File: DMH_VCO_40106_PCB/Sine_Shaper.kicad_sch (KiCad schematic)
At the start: 13 parts, among them Q5 2N3904, Q6 2N3904, U3 TL072

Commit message: Added Cermet 3296W fp to trimpots
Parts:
- RV10, RV9: footprint (none) -> Potentiometer_THT:Potentiometer_Bourns_3296W_Vertical
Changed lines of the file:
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@@
 			)
 		)
-		(property "Footprint" ""
+		(property "Footprint" "Potentiometer_THT:Potentiometer_Bourns_3296W_Vertical"
 			(at 120.65 115.57 0)
 			(effects
@@
 			)
 		)
-		(property "Footprint" ""
+		(property "Footprint" "Potentiometer_THT:Potentiometer_Bourns_3296W_Vertical"
 			(at 82.55 87.63 0)
 			(effects

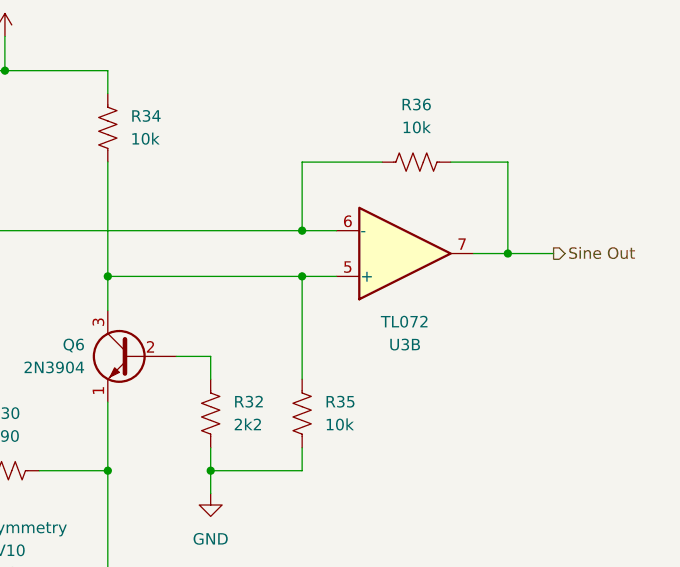
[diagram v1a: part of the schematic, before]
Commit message: Made U3 into TL074 instead of TL072
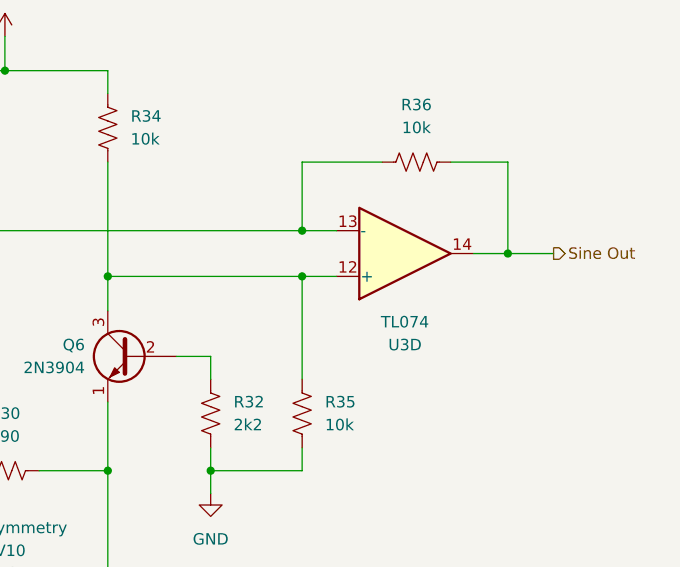
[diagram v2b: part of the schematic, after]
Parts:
- removed U3: TL072, Package_DIP:DIP-8_W7.62mm_Socket, symbol Amplifier_Operational:TL072
- added U3: TL074, symbol Amplifier_Operational:TL074
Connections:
- net Sine Out: now also U3.14
- net at Q5.3 (C), R33.2, R36.1: now also U3.13 (-)
- net at Q6.3 (C), R34.2, R35.1: now also U3.12 (+)
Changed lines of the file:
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@@
+	)
+	(symbol
+		(lib_id "Amplifier_Operational:TL074")
+		(at 165.1 76.2 0)
+		(mirror x)
+		(unit 4)
+		(exclude_from_sim no)
+		(in_bom yes)
+		(on_board yes)
+		(dnp no)
+		(property "Reference" "U3"
+			(at 165.1 86.36 0)
+			(effects
+				(font
+					(size 1.27 1.27)
+				)
+			)
+		)
+		(property "Value" "TL074"
+			(at 165.1 83.82 0)
+			(effects
+				(font
+					(size 1.27 1.27)
+				)
+			)
+		)
+		(property "Footprint" ""
+			(at 163.83 78.74 0)
+			(effects
+				(font
+					(size 1.27 1.27)
+				)
+				(hide yes)
+			)
+		)
+		(property "Datasheet" "http://www.ti.com/lit/ds/symlink/tl071.pdf"
+			(at 166.37 81.28 0)
+			(effects
+				(font
+					(size 1.27 1.27)
+				)
+				(hide yes)
+			)
+		)
+		(property "Description" "Quad Low-Noise JFET-Input Operational Amplifiers, DIP-14/SOIC-14"
+			(at 165.1 76.2 0)
+			(effects
+				(font
+					(size 1.27 1.27)
+				)
+				(hide yes)
+			)
+		)
+		(pin "9"
+		)
+		(pin "5"
+		)
+		(pin "8"
+		)
+		(pin "11"
+		)
+		(pin "10"
+		)
+		(pin "3"
+		)
+		(pin "4"
+		)
+		(pin "1"
+		)
+		(pin "12"
+		)
+		(pin "14"
+		)
+		(pin "13"
+		)
+		(pin "6"
+		)
+		(pin "2"
+		)
+		(pin "7"
+		)
+		(instances
+			(project ""
+				(path "/fefed352-c100-4617-bbfb-c55e7427b122/5d4fa276-24f5-484f-b50d-2ebe5f0666ef"
+					(reference "U3")
+					(unit 4)
+				)
+			)
+		)
 	)
 	(symbol
@@
 				)
 			)
-		)
-	)
-	(symbol
-		(lib_id "Amplifier_Operational:TL072")
-		(at 165.1 76.2 0)
-		(mirror x)
-		(unit 2)
-		(exclude_from_sim no)
-		(in_bom yes)
-		(on_board yes)
-		(dnp no)
-		(property "Reference" "U3"
-			(at 165.1 86.36 0)
-			(effects
-				(font
-					(size 1.27 1.27)
-				)
-			)
-		)
-		(property "Value" "TL072"
-			(at 165.1 83.82 0)
-			(effects
-				(font
-					(size 1.27 1.27)
-				)
-			)
-		)
-		(property "Footprint" "Package_DIP:DIP-8_W7.62mm_Socket"
-			(at 165.1 76.2 0)
-			(effects
-				(font
-					(size 1.27 1.27)
-				)
-				(hide yes)
-			)
-		)
-		(property "Datasheet" "http://www.ti.com/lit/ds/symlink/tl071.pdf"
-			(at 165.1 76.2 0)
-			(effects
-				(font
-					(size 1.27 1.27)
-				)
-				(hide yes)
-			)
-		)
-		(property "Description" "Dual Low-Noise JFET-Input Operational Amplifiers, DIP-8/SOIC-8"
-			(at 165.1 76.2 0)
-			(effects
-				(font
-					(size 1.27 1.27)
-				)
-				(hide yes)
-			)
-		)
-		(pin "2"
-		)
-		(pin "1"
-		)
-		(pin "7"
-		)
-		(pin "4"
-		)
-		(pin "6"
-		)
-		(pin "3"
-		)
-		(pin "5"
-		)
-		(pin "8"
-		)
-		(instances
-			(project "VCO mki PCB"
-				(path "/fefed352-c100-4617-bbfb-c55e7427b122/5d4fa276-24f5-484f-b50d-2ebe5f0666ef"
-					(reference "U3")
-					(unit 2)
-				)
-			)

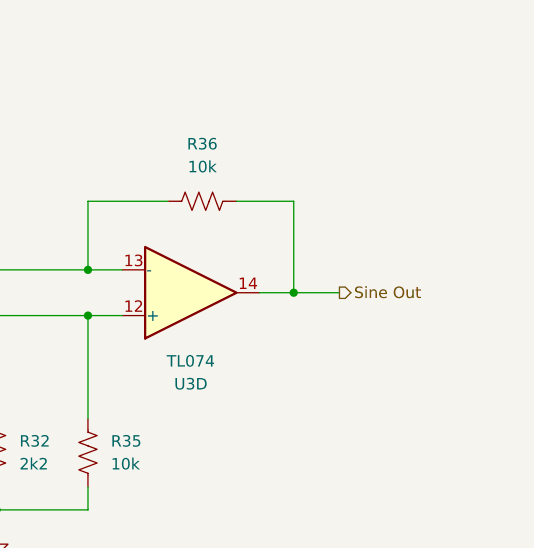
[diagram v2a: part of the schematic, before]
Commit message: Improved range of Coarse knob
... and allowed Centering knob to set C1=32,7Hz as root note with Coarse knob all the way CCW.
... and added 1kHz to Sine output.
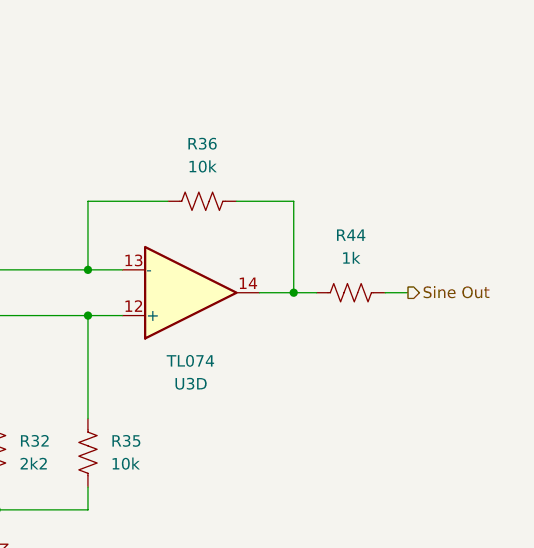
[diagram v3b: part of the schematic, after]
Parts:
- added R44: 1k, symbol Device:R_US
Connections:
- net Sine Out: now also R44.2; no longer R36.2, U3.14
- new net: R36.2, R44.1, U3.14
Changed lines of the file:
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@@
+	)
+	(junction
+		(at 132.08 100.33)
+		(diameter 0)
+		(color 0 0 0 0)
+	)
+	(junction
+		(at 143.51 100.33)
+		(diameter 0)
+		(color 0 0 0 0)
+	)
+	(junction
+		(at 76.2 87.63)
+		(diameter 0)
+		(color 0 0 0 0)
+	)
+	(junction
+		(at 109.22 100.33)
+		(diameter 0)
+		(color 0 0 0 0)
 	)
 	(junction
@@
 	)
 	(junction
-		(at 132.08 100.33)
-		(diameter 0)
-		(color 0 0 0 0)
-	)
-	(junction
-		(at 143.51 100.33)
-		(diameter 0)
-		(color 0 0 0 0)
-	)
-	(junction
-		(at 76.2 87.63)
-		(diameter 0)
-		(color 0 0 0 0)
-	)
-	(junction
-		(at 109.22 100.33)
-		(diameter 0)
-		(color 0 0 0 0)
-	)
-	(junction
 		(at 97.79 87.63)
 		(diameter 0)
@@
 	(wire
 		(pts
-			(xy 176.53 76.2) (xy 181.61 76.2)
+			(xy 186.69 76.2) (xy 189.23 76.2)
 		)
 		(stroke
@@
 		(pts
 			(xy 124.46 100.33) (xy 132.08 100.33)
+		)
+		(stroke
+			(width 0)
+			(type default)
+		)
+	)
+	(wire
+		(pts
+			(xy 176.53 76.2) (xy 179.07 76.2)
 		)
 		(stroke
@@
 	(hierarchical_label "Sine Out"
 		(shape output)
-		(at 181.61 76.2 0)
+		(at 189.23 76.2 0)
 		(fields_autoplaced yes)
 		(effects
@@
 					(unit 1)
 				)
+			)
+		)
+	)
+	(symbol
+		(lib_id "Device:R_US")
+		(at 182.88 76.2 90)
+		(unit 1)
+		(exclude_from_sim no)
+		(in_bom yes)
+		(on_board yes)
+		(dnp no)
+		(fields_autoplaced yes)
+		(property "Reference" "R44"
+			(at 182.88 69.85 90)
+			(effects
+				(font
+					(size 1.27 1.27)
+				)
+			)
+		)
+		(property "Value" "1k"
+			(at 182.88 72.39 90)
+			(effects
+				(font
+					(size 1.27 1.27)
+				)
+			)
+		)
+		(property "Footprint" ""
+			(at 183.134 75.184 90)
+			(effects
+				(font
+					(size 1.27 1.27)
+				)
+				(hide yes)
+			)
+		)
+		(property "Datasheet" "~"
+			(at 182.88 76.2 0)
+			(effects
+				(font
+					(size 1.27 1.27)
+				)
+				(hide yes)
+			)
+		)
+		(property "Description" "Resistor, US symbol"
+			(at 182.88 76.2 0)
+			(effects
+				(font
+					(size 1.27 1.27)
+				)
+				(hide yes)
+			)
+		)
+		(pin "2"
+		)
+		(pin "1"
+		)
+		(instances
+			(project "DMH_VCO_40106_PCB"
+				(path "/fefed352-c100-4617-bbfb-c55e7427b122/5d4fa276-24f5-484f-b50d-2ebe5f0666ef"
+					(reference "R44")
+					(unit 1)
+				)

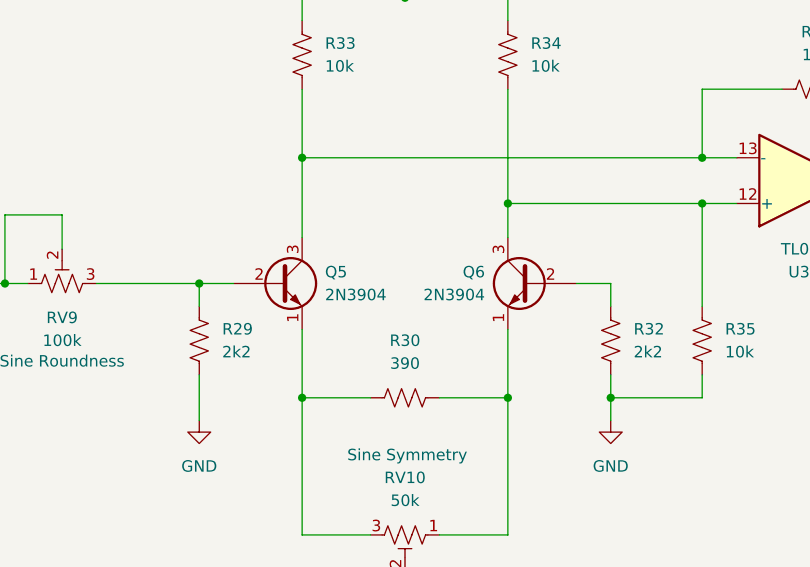
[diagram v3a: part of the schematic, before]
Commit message: Replaced 2N3904 with BC548
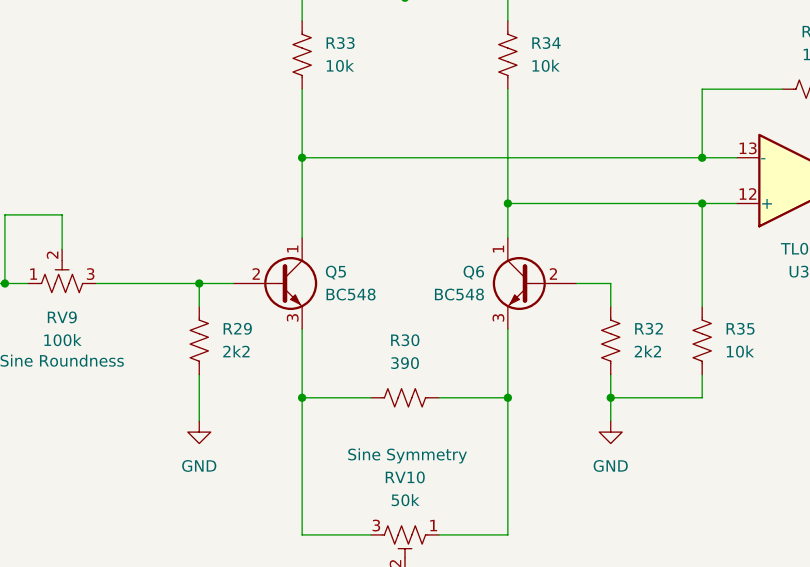
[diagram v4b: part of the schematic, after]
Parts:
- Q5, Q6: value 2N3904 -> BC548; symbol Transistor_BJT:2N3904 -> Transistor_BJT:BC548
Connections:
- net at R33.2, R36.1, U3.13 (-): now also Q5.1 (C); no longer Q5.3 (C)
- net at R30.2, RV10.1: now also Q6.3 (E); no longer Q6.1 (E)
- net at R30.1, RV10.3: now also Q5.3 (E); no longer Q5.1 (E)
- net at R34.2, R35.1, U3.12 (+): now also Q6.1 (C); no longer Q6.3 (C)
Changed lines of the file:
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@@
 	)
 	(symbol
-		(lib_id "Transistor_BJT:2N3904")
+		(lib_id "Transistor_BJT:BC548")
 		(at 106.68 87.63 0)
 		(unit 1)
@@
 			)
 		)
-		(property "Value" "2N3904"
+		(property "Value" "BC548"
 			(at 111.76 88.8999 0)
 			(effects
@@
 			)
 		)
-		(property "Datasheet" "https://www.onsemi.com/pub/Collateral/2N3903-D.PDF"
+		(property "Datasheet" "https://www.onsemi.com/pub/Collateral/BC550-D.pdf"
 			(at 106.68 87.63 0)
 			(effects
@@
 			)
 		)
-		(property "Description" "0.2A Ic, 40V Vce, Small Signal NPN Transistor, TO-92"
+		(property "Description" "0.1A Ic, 30V Vce, Small Signal NPN Transistor, TO-92"
 			(at 106.68 87.63 0)
 			(effects
@@
 	)
 	(symbol
-		(lib_id "Transistor_BJT:2N3904")
+		(lib_id "Transistor_BJT:BC548")
 		(at 134.62 87.63 0)
 		(mirror y)
@@
 			)
 		)
-		(property "Value" "2N3904"
+		(property "Value" "BC548"
 			(at 129.54 88.8999 0)
 			(effects
@@
 			)
 		)
-		(property "Datasheet" "https://www.onsemi.com/pub/Collateral/2N3903-D.PDF"
+		(property "Datasheet" "https://www.onsemi.com/pub/Collateral/BC550-D.pdf"
 			(at 134.62 87.63 0)
 			(effects
@@
 			)
 		)
-		(property "Description" "0.2A Ic, 40V Vce, Small Signal NPN Transistor, TO-92"
+		(property "Description" "0.1A Ic, 30V Vce, Small Signal NPN Transistor, TO-92"
 			(at 134.62 87.63 0)
 			(effects

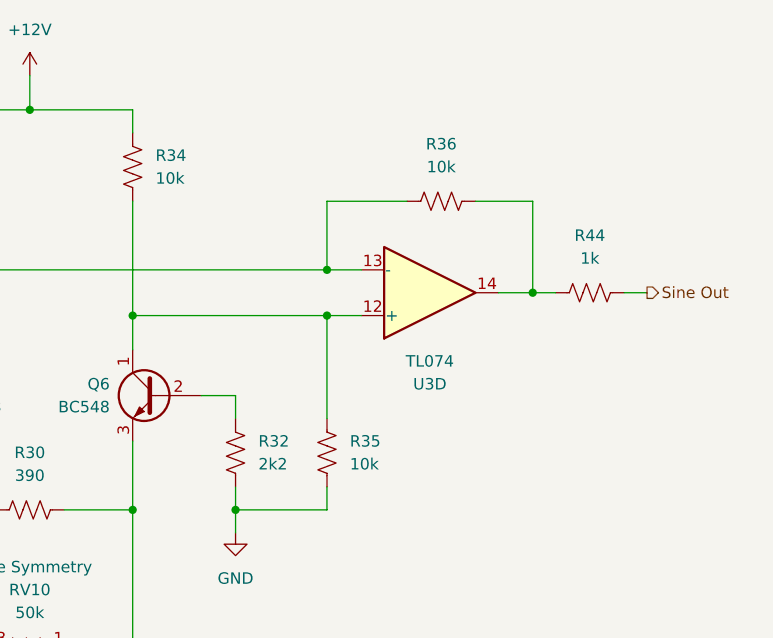
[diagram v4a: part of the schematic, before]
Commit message: Adjusted all output gains to 10Vpp
... and added buffer stages for Sawtooth Out and Triangle Out in order to avoid modifying Triangle and Sine wafeform characteristics when connecting Sawtooth Out and Triangle Out to other modules.
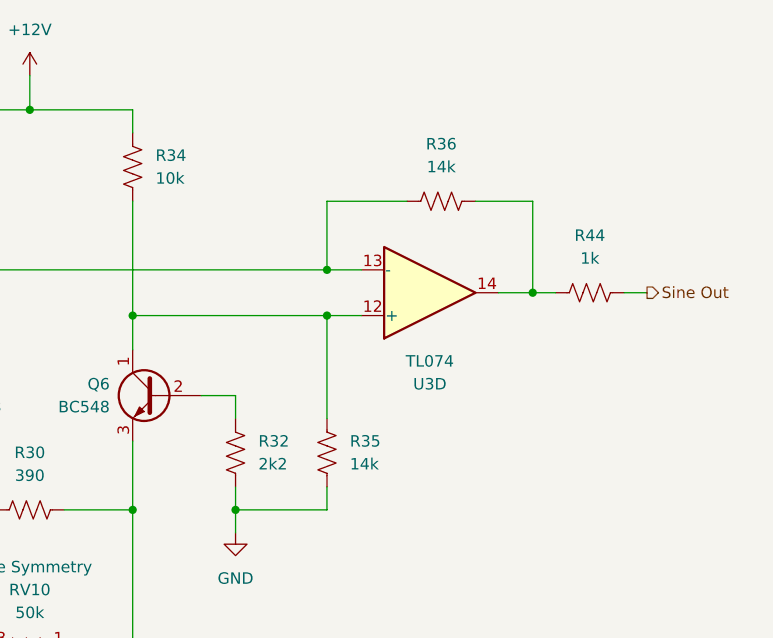
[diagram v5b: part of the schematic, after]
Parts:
- R35, R36: value 10k -> 14k
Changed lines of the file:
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@@
 			)
 		)
-		(property "Value" "10k"
+		(property "Value" "14k"
 			(at 166.37 62.23 90)
 			(effects
@@
 			)
 		)
-		(property "Value" "10k"
+		(property "Value" "14k"
 			(at 156.21 95.2499 0)
 			(effects

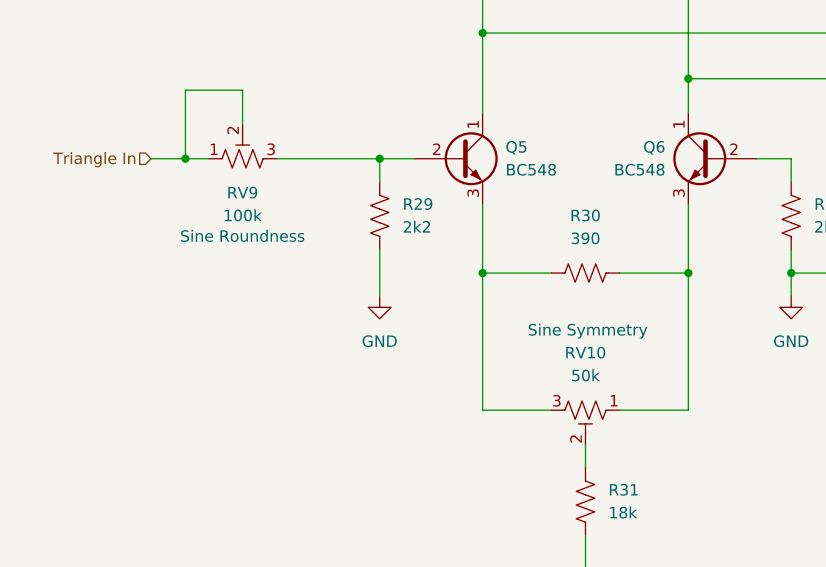
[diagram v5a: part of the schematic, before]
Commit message: Updated Tuner
- Changed uC to ATtiny4313
- Added LEDs
- Created "function" field and updated all jacks, switches and pots
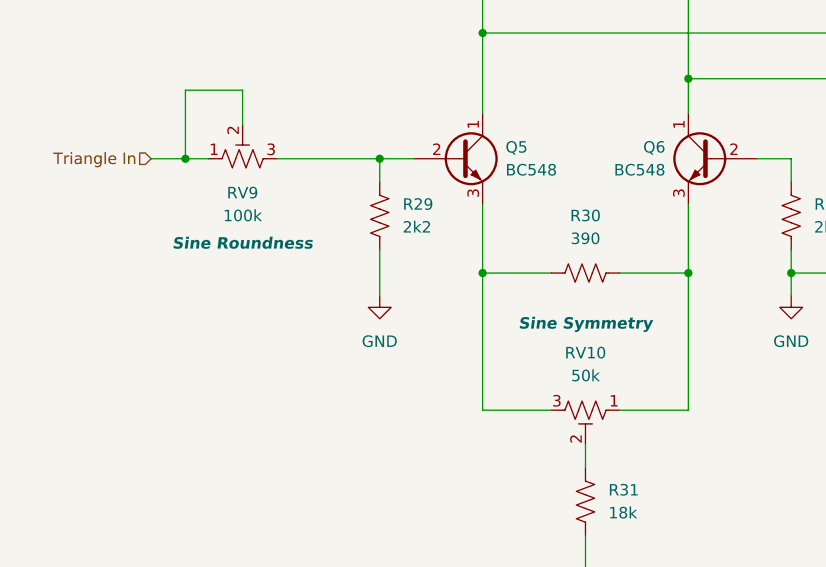
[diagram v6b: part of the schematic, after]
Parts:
- RV10: Function (none) -> Sine Symmetry
- RV9: Function (none) -> Sine Roundness
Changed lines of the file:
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@@
 			)
 		)
-		(property "Description" "Sine Symmetry"
+		(property "Description" ""
 			(at 120.904 106.68 90)
 			(effects
 				(font
 					(size 1.27 1.27)
+				)
+				(hide yes)
+			)
+		)
+		(property "Function" "Sine Symmetry"
+			(at 120.65 105.918 90)
+			(effects
+				(font
+					(size 1.27 1.27)
+					(bold yes)
+					(italic yes)
 				)
 			)
@@
 			)
 		)
-		(property "Description" "Sine Roundness"
+		(property "Description" ""
 			(at 82.55 96.266 90)
 			(effects
@@
 					(size 1.27 1.27)
 				)
-			)
+				(hide yes)
+			)
+		)
+		(property "Function" "Sine Roundness"
+			(at 82.55 97.028 90)
+			(effects
+				(font
+					(size 1.27 1.27)
+					(bold yes)
+					(italic yes)
+				)
+			)

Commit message: Fixed trimpot fp linking
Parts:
- U3: footprint (none) -> Package_DIP:DIP-14_W7.62mm_Socket
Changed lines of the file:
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@@
 			)
 		)
-		(property "Footprint" ""
+		(property "Footprint" "Package_DIP:DIP-14_W7.62mm_Socket"
 			(at 163.83 78.74 0)
 			(effects

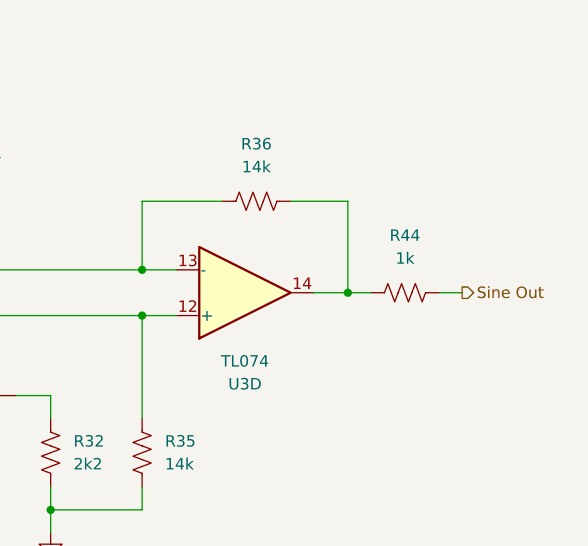
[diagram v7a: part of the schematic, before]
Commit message: Started positioning components on PCB
Moving some input resistores from main PCB to Jacks PCB
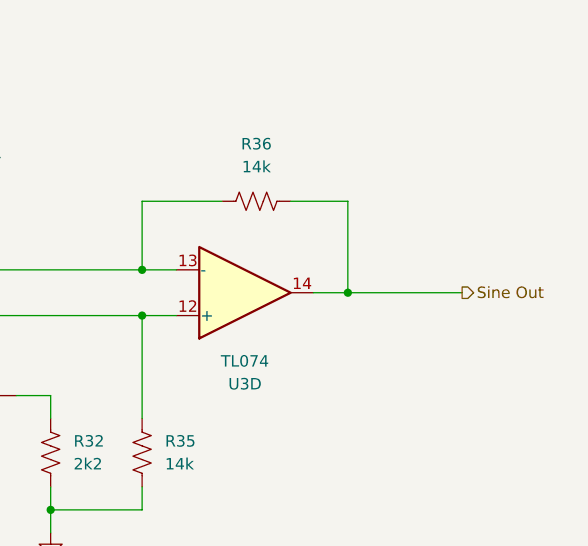
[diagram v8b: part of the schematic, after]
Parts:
- removed R44: 1k, symbol Device:R_US
- Q5, Q6: footprint Package_TO_SOT_THT:TO-92_Inline -> Package_TO_SOT_THT:TO-92_Inline_Wide
- R29, R30, R31, R32, R33, R34, R35, R36: footprint (none) -> Resistor_THT:R_Axial_DIN0207_L6.3mm_D2.5mm_P7.62mm_Horizontal
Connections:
- net Sine Out: now also R36.2, U3.14
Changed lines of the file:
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@@
-	(wire
-		(pts
-			(xy 186.69 76.2) (xy 189.23 76.2)
-		)
-		(stroke
-			(width 0)
-			(type default)
-		)
-	)
 	(wire
 		(pts
@@
 	(wire
 		(pts
-			(xy 176.53 76.2) (xy 179.07 76.2)
+			(xy 176.53 76.2) (xy 189.23 76.2)
 		)
 		(stroke
@@
 			)
 		)
-		(property "Footprint" ""
+		(property "Footprint" "Resistor_THT:R_Axial_DIN0207_L6.3mm_D2.5mm_P7.62mm_Horizontal"
 			(at 144.526 94.234 90)
 			(effects
@@
 			)
 		)
-		(property "Footprint" ""
+		(property "Footprint" "Resistor_THT:R_Axial_DIN0207_L6.3mm_D2.5mm_P7.62mm_Horizontal"
 			(at 166.624 65.024 90)
 			(effects
@@
 	(symbol
 		(lib_id "Device:R_US")
-		(at 182.88 76.2 90)
-		(unit 1)
-		(exclude_from_sim no)
-		(in_bom yes)
-		(on_board yes)
-		(dnp no)
-		(fields_autoplaced yes)
-		(property "Reference" "R44"
-			(at 182.88 69.85 90)
-			(effects
-				(font
-					(size 1.27 1.27)
-				)
-			)
-		)
-		(property "Value" "1k"
-			(at 182.88 72.39 90)
-			(effects
-				(font
-					(size 1.27 1.27)
-				)
-			)
-		)
-		(property "Footprint" ""
-			(at 183.134 75.184 90)
-			(effects
-				(font
-					(size 1.27 1.27)
-				)
-				(hide yes)
-			)
-		)
-		(property "Datasheet" "~"
-			(at 182.88 76.2 0)
-			(effects
-				(font
-					(size 1.27 1.27)
-				)
-				(hide yes)
-			)
-		)
-		(property "Description" "Resistor, US symbol"
-			(at 182.88 76.2 0)
-			(effects
-				(font
-					(size 1.27 1.27)
-				)
-				(hide yes)
-			)
-		)
-		(pin "2"
-		)
-		(pin "1"
-		)
-		(instances
-			(project "DMH_VCO_40106_PCB"
-				(path "/fefed352-c100-4617-bbfb-c55e7427b122/5d4fa276-24f5-484f-b50d-2ebe5f0666ef"
-					(reference "R44")
-					(unit 1)
-				)
-			)
-		)
-	)
-	(symbol
-		(lib_id "Device:R_US")
 		(at 120.65 100.33 90)
 		(unit 1)
@@
 			)
 		)
-		(property "Footprint" ""
+		(property "Footprint" "Resistor_THT:R_Axial_DIN0207_L6.3mm_D2.5mm_P7.62mm_Horizontal"
 			(at 120.904 99.314 90)
 			(effects
@@
 			)
 		)
-		(property "Footprint" ""
+		(property "Footprint" "Resistor_THT:R_Axial_DIN0207_L6.3mm_D2.5mm_P7.62mm_Horizontal"
 			(at 98.806 94.234 90)
 			(effects
@@
 			)
 		)
-		(property "Footprint" ""
+		(property "Footprint" "Resistor_THT:R_Axial_DIN0207_L6.3mm_D2.5mm_P7.62mm_Horizontal"
 			(at 110.236 62.484 90)
 			(effects
@@
 			)
 		)
-		(property "Footprint" "Package_TO_SOT_THT:TO-92_Inline"
+		(property "Footprint" "Package_TO_SOT_THT:TO-92_Inline_Wide"
 			(at 111.76 89.535 0)
 			(effects
@@
 			)
 		)
-		(property "Footprint" "Package_TO_SOT_THT:TO-92_Inline"
+		(property "Footprint" "Package_TO_SOT_THT:TO-92_Inline_Wide"
 			(at 129.54 89.535 0)
 			(effects
@@
 			)
 		)
-		(property "Footprint" ""
+		(property "Footprint" "Resistor_THT:R_Axial_DIN0207_L6.3mm_D2.5mm_P7.62mm_Horizontal"
 			(at 119.634 125.476 90)
 			(effects
@@
 			)
 		)
-		(property "Footprint" ""
+		(property "Footprint" "Resistor_THT:R_Axial_DIN0207_L6.3mm_D2.5mm_P7.62mm_Horizontal"
 			(at 154.686 94.234 90)
 			(effects
@@
 			)
 		)
-		(property "Footprint" ""
+		(property "Footprint" "Resistor_THT:R_Axial_DIN0207_L6.3mm_D2.5mm_P7.62mm_Horizontal"
 			(at 133.096 62.484 90)
 			(effects
